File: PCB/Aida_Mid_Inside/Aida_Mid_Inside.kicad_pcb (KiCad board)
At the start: 2 copper layers, 50.3 x 61.6 mm, 16 parts

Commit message: プレート作成中
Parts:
- moved H1 1.19 mm to (123.8, 36.3)
- moved H4 1.19 mm to (147.6, 52.4)
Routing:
- net COL_4_from_Base: track 38.0 -> 38.9 mm
- net GND: vias 12 -> 15
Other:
- outline, holes or cut-outs redrawn
- board text added: "Mid PCB outline"

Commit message: LED位置、とりあえず決定。
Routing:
- net COL_4_from_Base: track 38.9 -> 41.3 mm, vias 2 -> 1
- net COL_4_to_Base: track 66.9 -> 65.8 mm, vias 1 -> 0
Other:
- outline, holes or cut-outs redrawn
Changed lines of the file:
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@@
 		(allow_soldermask_bridges_in_footprints no)
 		(tenting front back)
-		(grid_origin 23.8125 23.8125)
+		(grid_origin 23.8125 23.812492)
 		(pcbplotparams
 			(layerselection 0x00000000_00000000_55555555_5755f5ff)
@@
 	)
 	(gr_line
-		(start 143.901665 57.435967)
-		(end 147.801665 57.435967)
+		(start 141.375 57.531242)
+		(end 144.375 57.531242)
 		(stroke
 			(width 0.05)
@@
 	)
 	(gr_line
-		(start 147.801665 69.960975)
-		(end 143.901665 69.960975)
+		(start 144.375 71.031242)
+		(end 141.375 71.031242)
 		(stroke
 			(width 0.05)
@@
 	)
 	(gr_line
-		(start 143.901665 57.435967)
-		(end 143.901665 69.960975)
+		(start 141.375 57.531242)
+		(end 141.375 71.031242)
 		(stroke
 			(width 0.05)
@@
 	)
 	(gr_line
-		(start 147.801665 57.435967)
-		(end 147.801665 69.960975)
+		(start 144.375 57.531242)
+		(end 144.375 71.031242)
 		(stroke
 			(width 0.05)
@@
 		)
 	)
-	(segment
-		(start 147.637604 53.57815)
-		(end 145.24685 53.57815)
-		(width 0.381)
-		(layer "F.Cu")
-		(net 1)
-	)
-	(segment
-		(start 125.775 72.25)
-		(end 127.341498 70.6835)
-		(width 0.381)
-		(layer "F.Cu")
-		(net 1)
+	(dimension
+		(type orthogonal)
+		(layer "Dwgs.User")
+		(pts
+			(xy 141.375 57.531242) (xy 144.375 57.531242)
+		)
+		(height -2)
+		(orientation 0)
+		(format
+			(prefix "")
+			(suffix "")
+			(units 3)
+			(units_format 0)
+			(precision 4)
+			(suppress_zeroes yes)
+		)
+		(style
+			(thickness 0.1)
+			(arrow_length 1.27)
+			(text_position_mode 0)
+			(arrow_direction outward)
+			(extension_height 0.58642)
+			(extension_offset 0.5)
+			(keep_text_aligned yes)
+		)
+		(gr_text "3"
+			(at 142.875 54.381242 0)
+			(layer "Dwgs.User")
+			(effects
+				(font
+					(size 1 1)
+					(thickness 0.15)
+				)
+			)
+		)
 	)
-	(segment
-		(start 145.24685 53.57815)
-		(end 140.8125 58.0125)
-		(width 0.381)
-		(layer "F.Cu")
-		(net 1)
+	(dimension
+		(type orthogonal)
+		(layer "Dwgs.User")
+		(pts
+			(xy 141.375 57.531242) (xy 141.375 71.031242)
+		)
+		(height -1)
+		(orientation 1)
+		(format
+			(prefix "")
+			(suffix "")
+			(units 3)
+			(units_format 0)
+			(precision 4)
+			(suppress_zeroes yes)
+		)
+		(style
+			(thickness 0.1)
+			(arrow_length 1.27)
+			(text_position_mode 0)
+			(arrow_direction outward)
+			(extension_height 0.58642)
+			(extension_offset 0.5)
+			(keep_text_aligned yes)
+		)
+		(gr_text "13.5"
+			(at 139.225 64.281242 90)
+			(layer "Dwgs.User")
+			(effects
+				(font
+					(size 1 1)
+					(thickness 0.15)
+				)
+			)
+		)
 	)
 	(segment
-		(start 140.8125 68.965274)
-		(end 140.765274 69.0125)
+		(start 147.637604 53.57815)
+		(end 147.637604 52.387524)
 		(width 0.381)
 		(layer "F.Cu")
@@
 	)
 	(segment
-		(start 125.775 72.975)
-		(end 125.775 72.25)
+		(start 125.775 72.431242)
+		(end 125.775 72.975)
 		(width 0.381)
 		(layer "F.Cu")
@@
 	)
 	(segment
-		(start 140.8125 58.0125)
-		(end 140.8125 68.965274)
+		(start 127.475 70.731242)
+		(end 125.775 72.431242)
 		(width 0.381)
 		(layer "F.Cu")
@@
 	)
 	(via
-		(at 127.341498 70.6835)
+		(at 127.475 70.731242)
 		(size 0.6)
 		(drill 0.3)
@@
 		(net 1)
 	)
-	(via
-		(at 140.765274 69.0125)
-		(size 0.6)
-		(drill 0.3)
-		(layers "F.Cu" "B.Cu")
+	(segment
+		(start 139.618718 52.387524)
+		(end 131.529 60.477242)
+		(width 0.381)
+		(layer "B.Cu")
 		(net 1)
 	)
 	(segment
 		(start 129.391696 70.6835)
-		(end 127.341498 70.6835)
+		(end 127.522742 70.6835)
 		(width 0.381)
 		(layer "B.Cu")
@@
 	)
 	(segment
-		(start 131.3875 73.0125)
-		(end 131.3875 72.679304)
+		(start 147.637604 52.387524)
+		(end 139.618718 52.387524)
 		(width 0.381)
 		(layer "B.Cu")
@@
 	)
 	(segment
+		(start 131.529 60.477242)
+		(end 131.529 72.871)
+		(width 0.381)
+		(layer "B.Cu")
+		(net 1)
+	)
+	(segment
 		(start 131.3875 73.0125)
-		(end 133.8125 73.0125)
+		(end 131.3875 72.679304)
 		(width 0.381)
 		(layer "B.Cu")
@@
 	)
 	(segment
-		(start 137.8125 69.0125)
-		(end 140.765274 69.0125)
+		(start 127.522742 70.6835)
+		(end 127.475 70.731242)
 		(width 0.381)
 		(layer "B.Cu")
@@
 	)
 	(segment
-		(start 133.8125 73.0125)
-		(end 137.8125 69.0125)
+		(start 131.529 72.871)
+		(end 131.3875 73.0125)
 		(width 0.381)
 		(layer "B.Cu")
@@
 	)
 	(segment
-		(start 136.8625 38.754795)
-		(end 136.8625 68.24375)
+		(start 120.3875 69.075)
+		(end 120.979 68.4835)
 		(width 0.381)
 		(layer "F.Cu")
@@
 	)
 	(segment
-		(start 136.8625 70.425)
-		(end 136.8625 68.24375)
+		(start 134.921 68.4835)
+		(end 136.8625 70.425)
 		(width 0.381)
 		(layer "F.Cu")
@@
 	)
 	(segment
-		(start 139.303222 36.314073)
-		(end 136.8625 38.754795)
+		(start 139.303222 67.984278)
+		(end 136.8625 70.425)
 		(width 0.381)
 		(layer "F.Cu")
 		(net 4)
 	)
-	(via
-		(at 136.8625 68.24375)
-		(size 0.6)
-		(drill 0.3)
-		(layers "F.Cu" "B.Cu")
-		(net 4)
-	)
 	(segment
-		(start 120.8 69.4875)
-		(end 121.9935 68.294)
+		(start 124.391696 68.4835)
+		(end 125.529 69.620804)
 		(width 0.381)
-		(layer "B.Cu")
-		(net 4)
-	)
-	(segment
-		(start 147.637604 73.818792)
-		(end 146.781553 73.818792)
-		(width 0.381)
-		(layer "B.Cu")
-		(net 4)
-	)
-	(segment
-		(start 131.615203 69.651601)
-		(end 133.023054 68.24375)
-		(width 0.381)
-		(layer "B.Cu")
+		(layer "F.Cu")
 		(net 4)
 	)
 	(segment
-		(start 125.651601 69.651601)
-		(end 131.615203 69.651601)
+		(start 125.529 69.620804)
+		(end 131.646 69.620804)
 		(width 0.381)
-		(layer "B.Cu")
+		(layer "F.Cu")
 		(net 4)
 	)
 	(segment
-		(start 133.023054 68.24375)
-		(end 136.8625 68.24375)
+		(start 120.979 68.4835)
+		(end 124.391696 68.4835)
 		(width 0.381)
-		(layer "B.Cu")
+		(layer "F.Cu")
 		(net 4)
 	)
 	(segment
-		(start 120.8 70.475)
-		(end 120.8 69.4875)
+		(start 140.256292 73.818792)
+		(end 136.8625 70.425)
 		(width 0.381)
-		(layer "B.Cu")
+		(layer "F.Cu")
 		(net 4)
 	)
 	(segment
-		(start 141.206511 68.24375)
-		(end 136.8625 68.24375)
+		(start 132.783304 68.4835)
+		(end 134.921 68.4835)
 		(width 0.381)
-		(layer "B.Cu")
+		(layer "F.Cu")
 		(net 4)
 	)
 	(segment
-		(start 146.781553 73.818792)
-		(end 141.206511 68.24375)
+		(start 131.646 69.620804)
+		(end 132.783304 68.4835)
 		(width 0.381)
-		(layer "B.Cu")
+		(layer "F.Cu")
 		(net 4)
 	)
 	(segment
-		(start 121.9935 68.294)
-		(end 124.294 68.294)
+		(start 139.303222 36.314073)
+		(end 139.303222 67.984278)
 		(width 0.381)
-		(layer "B.Cu")
+		(layer "F.Cu")
 		(net 4)
 	)
 	(segment
-		(start 124.294 68.294)
-		(end 125.651601 69.651601)
+		(start 147.637604 73.818792)
+		(end 140.256292 73.818792)
 		(width 0.381)
-		(layer "B.Cu")
+		(layer "F.Cu")
 		(net 4)
 	)
@@
 	)
 	(segment
-		(start 135.159262 89.6125)
-		(end 138.795696 89.6125)
+		(start 135.157784 89.613978)
+		(end 135.159262 89.6125)
 		(width 0.381)
 		(layer "B.Cu")
@@
 	)
 	(segment
-		(start 135.157784 89.613978)
-		(end 135.159262 89.6125)
+		(start 140.9125 91.168742)
+		(end 140.9125 92.0625)
 		(width 0.381)
 		(layer "B.Cu")
@@
 	)
 	(segment
-		(start 138.795696 89.6125)
-		(end 140.9125 91.729304)
+		(start 135.159262 89.6125)
+		(end 139.356258 89.6125)
 		(width 0.381)
 		(layer "B.Cu")
@@
 	)
 	(segment
-		(start 140.9125 91.729304)
-		(end 140.9125 92.0625)
+		(start 139.356258 89.6125)
+		(end 140.9125 91.168742)
 		(width 0.381)
 		(layer "B.Cu")
@@
 		)
 	)
+	(group ""
+		(members "30b967c6-47ee-4314-aa3e-2ab2c3127d4e" "9c83c8d8-1a02-40a3-85f6-0ebe3c686e59"
+			"9f04287f-cfcd-4da3-97c0-38c89c8849d0" "9f1fa874-ab79-46f0-ade8-69dd9abeedb4"
+			"a251b266-c423-4cf9-8e4d-5526a435a28b" "e51604d4-8483-49e3-b748-a80548c7b92b"
+		)
+	)

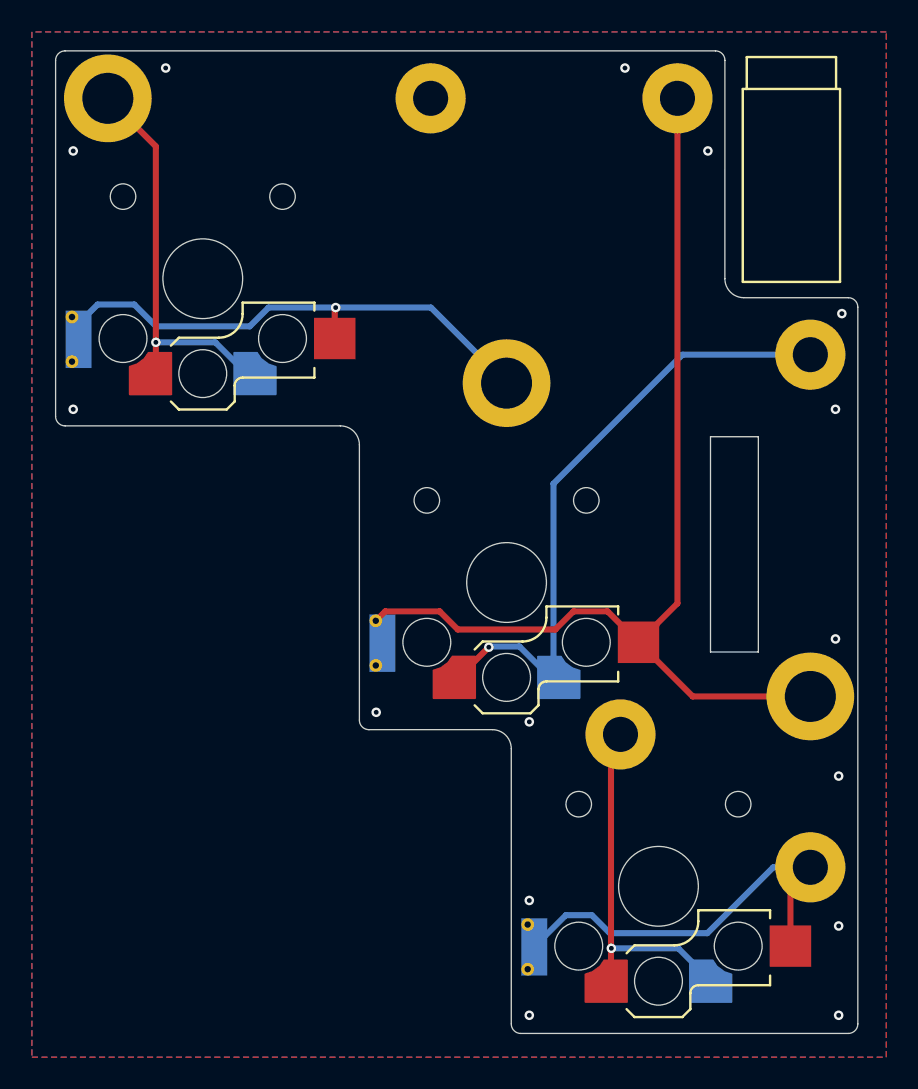
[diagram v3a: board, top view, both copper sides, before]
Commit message: テストポイントを追加、配置した。
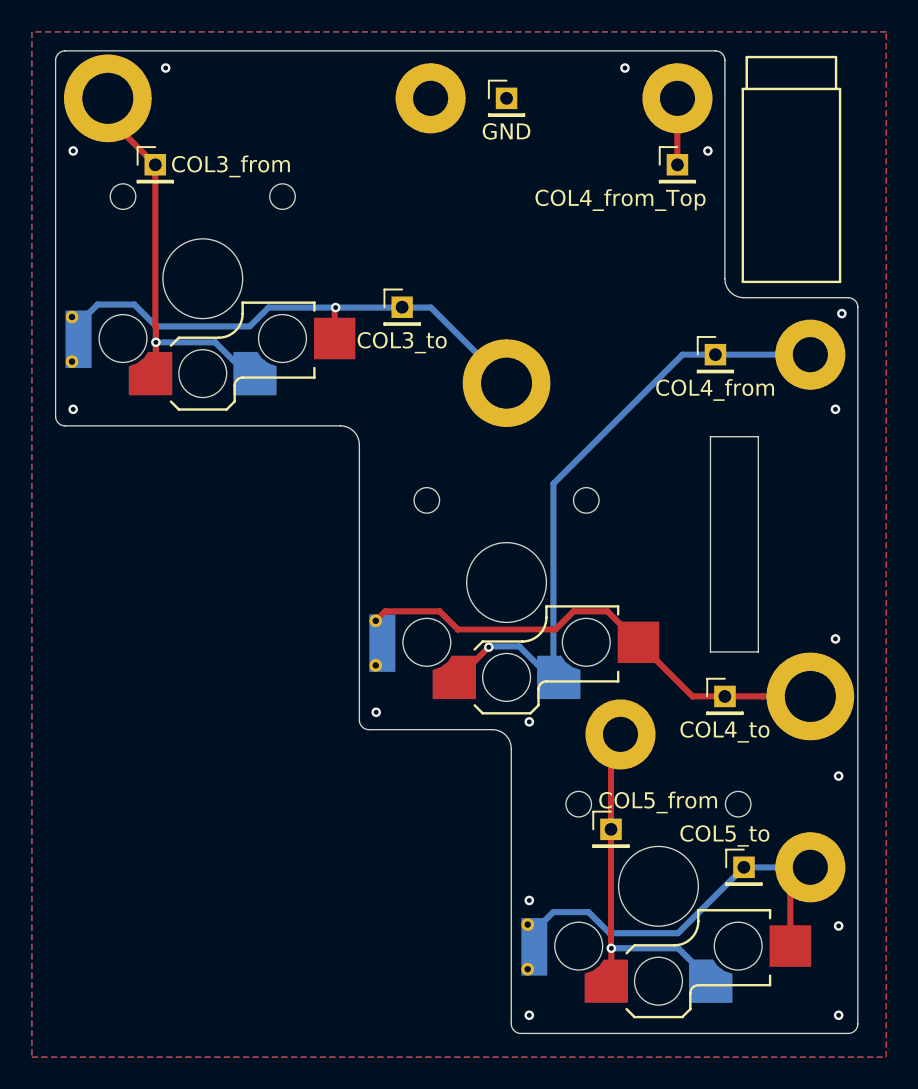
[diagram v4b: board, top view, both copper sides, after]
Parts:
- added TP1: GND, Connector_PinHeader_2.00mm:PinHeader_1x01_P2.00mm_Vertical, F.Cu at (128.6, 36.3)
- added TP2: COL3_from, Connector_PinHeader_2.00mm:PinHeader_1x01_P2.00mm_Vertical, F.Cu at (106.6, 40.5)
- added TP3: COL3_to, Connector_PinHeader_2.00mm:PinHeader_1x01_P2.00mm_Vertical, F.Cu at (122.0, 49.4)
- added TP4: COL4_from, Connector_PinHeader_2.00mm:PinHeader_1x01_P2.00mm_Vertical, F.Cu at (141.7, 52.4)
- added TP5: COL4_to, Connector_PinHeader_2.00mm:PinHeader_1x01_P2.00mm_Vertical, F.Cu at (142.3, 73.8)
- added TP6: COL5_from, Connector_PinHeader_2.00mm:PinHeader_1x01_P2.00mm_Vertical, F.Cu at (135.1, 82.2)
- added TP7: COL5_to, Connector_PinHeader_2.00mm:PinHeader_1x01_P2.00mm_Vertical, F.Cu at (143.5, 84.5)
- added TP8: COL4_from_Top, Connector_PinHeader_2.00mm:PinHeader_1x01_P2.00mm_Vertical, F.Cu at (139.3, 40.5)
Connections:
- H8 pad 1: COL_4_to_Base -> COL_4_from_Top_to_Base
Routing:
- net COL_4_to_Base: track 65.8 -> 30.6 mm
- net COL_4_from_Top_to_Base: track 0.00 -> 4.17 mm
- net COL_5_to_Base: track 25.8 -> 26.5 mm

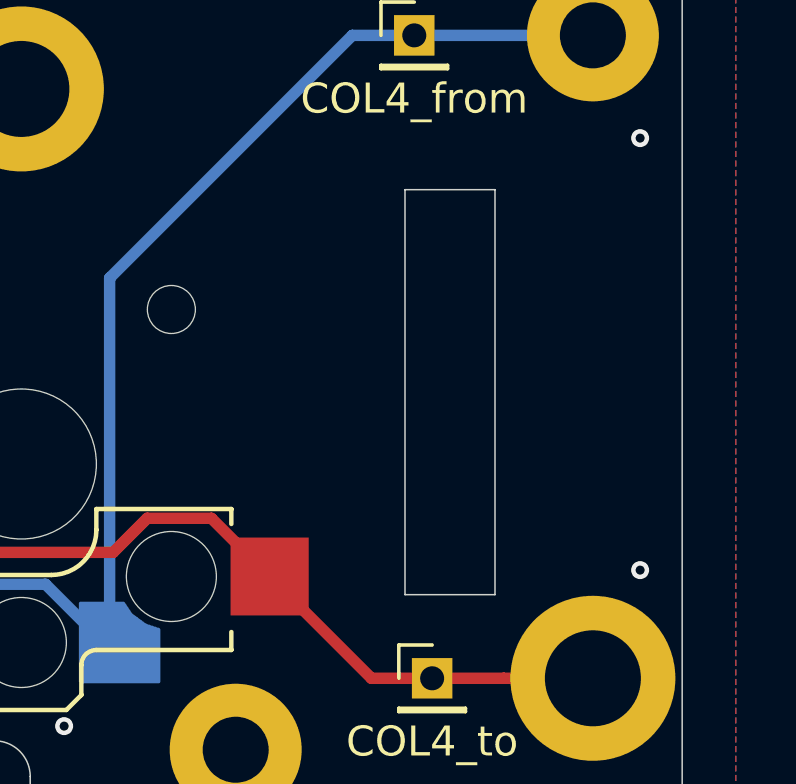
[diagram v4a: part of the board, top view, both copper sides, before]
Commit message: 原点ガイドを追加。基板Mid_InsideのLED穴形状調整
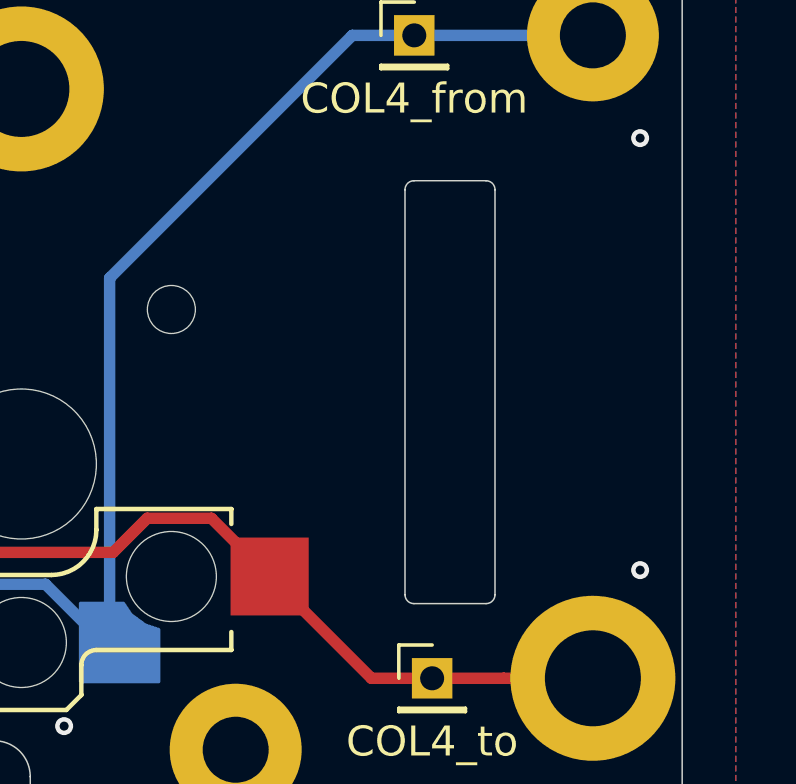
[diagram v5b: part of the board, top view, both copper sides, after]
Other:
- outline, holes or cut-outs redrawn
- board text added: "Center Origin"
- board text added: "Grid Origin"
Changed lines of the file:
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@@
 	)
 	(gr_line
-		(start 141.375 57.531242)
-		(end 144.375 57.531242)
+		(start 141.67265 57.233592)
+		(end 144.07735 57.233592)
 		(stroke
 			(width 0.05)
@@
 	)
 	(gr_arc
+		(start 144.375 71.031242)
+		(mid 144.28782 71.241712)
+		(end 144.07735 71.328892)
+		(stroke
+			(width 0.05)
+			(type default)
+		)
+		(layer "Edge.Cuts")
+	)
+	(gr_arc
 		(start 100.3086 33.9326)
 		(mid 100.482942 33.511677)
@@
 		(layer "Edge.Cuts")
 	)
-	(gr_line
-		(start 144.375 71.031242)
+	(gr_arc
+		(start 141.67265 71.328892)
+		(mid 141.46218 71.241712)
 		(end 141.375 71.031242)
+		(stroke
+			(width 0.05)
+			(type default)
+		)
+		(layer "Edge.Cuts")
+	)
+	(gr_line
+		(start 144.07735 71.328892)
+		(end 141.67265 71.328892)
 		(stroke
 			(width 0.05)
@@
 		(layer "Edge.Cuts")
 	)
+	(gr_arc
+		(start 141.375 57.531242)
+		(mid 141.46218 57.320772)
+		(end 141.67265 57.233592)
+		(stroke
+			(width 0.05)
+			(type default)
+		)
+		(layer "Edge.Cuts")
+	)
+	(gr_arc
+		(start 144.07735 57.233592)
+		(mid 144.28782 57.320772)
+		(end 144.375 57.531242)
+		(stroke
+			(width 0.05)
+			(type default)
+		)
+		(layer "Edge.Cuts")
+	)
 	(gr_line
 		(start 128.882903 77.09185)
@@
 		(locked yes)
 		(layer "Edge.Cuts")
+	)
+	(gr_circle
+		(center 152.4 23.812492)
+		(end 153.590625 23.812492)
+		(stroke
+			(width 0.1)
+			(type default)
+		)
+		(fill no)
+		(layer "User.1")
+	)
+	(gr_line
+		(start 152.4 21.431242)
+		(end 152.4 26.193742)
+		(stroke
+			(width 0.1)
+			(type default)
+		)
+		(layer "User.1")
+	)
+	(gr_line
+		(start 21.43125 23.812492)
+		(end 26.19375 23.812492)
+		(stroke
+			(width 0.1)
+			(type default)
+		)
+		(layer "User.1")
+	)
+	(gr_line
+		(start 150.01875 23.812492)
+		(end 154.78125 23.812492)
+		(stroke
+			(width 0.1)
+			(type default)
+		)
+		(layer "User.1")
+	)
+	(gr_line
+		(start 23.8125 21.431242)
+		(end 23.8125 26.193742)
+		(stroke
+			(width 0.1)
+			(type default)
+		)
+		(layer "User.1")
+	)
+	(gr_circle
+		(center 23.8125 23.812492)
+		(end 25.003125 23.812492)
+		(stroke
+			(width 0.1)
+			(type default)
+		)
+		(fill no)
+		(layer "User.1")
 	)
 	(gr_text "Top PCB outline"
@@
 				(size 2 2)
 				(thickness 0.25)
+			)
+			(justify left bottom)
+		)
+	)
+	(gr_text "Grid Origin"
+		(at 20.240625 21.431242 0)
+		(layer "User.1")
+		(effects
+			(font
+				(size 1 1)
+				(thickness 0.15)
+			)
+			(justify left bottom)
+		)
+	)
+	(gr_text "Center Origin"
+		(at 148.828125 21.431242 0)
+		(layer "User.1")
+		(effects
+			(font
+				(size 1 1)
+				(thickness 0.15)
 			)
 			(justify left bottom)
@@
 	)
 	(group ""
-		(members "30b967c6-47ee-4314-aa3e-2ab2c3127d4e" "9c83c8d8-1a02-40a3-85f6-0ebe3c686e59"
+		(members "30b967c6-47ee-4314-aa3e-2ab2c3127d4e" "8da4108f-a7d7-4648-9480-3ab31f62fc9a"
+			"98a36b7b-e52f-494a-92c7-36c8a0a49cf5" "9c83c8d8-1a02-40a3-85f6-0ebe3c686e59"
 			"9f04287f-cfcd-4da3-97c0-38c89c8849d0" "9f1fa874-ab79-46f0-ade8-69dd9abeedb4"
-			"a251b266-c423-4cf9-8e4d-5526a435a28b" "e51604d4-8483-49e3-b748-a80548c7b92b"
+			"a251b266-c423-4cf9-8e4d-5526a435a28b" "b7f7d34b-47ca-4c86-8af2-f129ddcb246e"
+			"c89a7be0-8ec1-430a-af72-4761bc8d12c6" "e51604d4-8483-49e3-b748-a80548c7b92b"
 		)
 	)
@@
 		)
 	)
+	(group ""
+		(members "0d4ce8d2-d722-4ce7-8256-3333df4c33cc" "456ce0c4-90f3-4929-af18-fe6f7d69b78b"
+			"99fb3dae-9313-48c1-a0ae-9e57fc24b395" "d0ca1a3d-e71e-4370-94c3-9dffcacabe26"
+		)
+	)
+	(group ""
+		(members "753e5ebe-7735-42e4-b0fa-1daf63716b6c" "8fdd3093-8553-4b9e-b5b7-4e39a5a2a25a"
+			"d419bd74-2eb2-4d4c-8853-d5ee2cf8ba9a" "dde25f33-d434-4f71-8e6b-d175555132ea"
+		)
+	)
